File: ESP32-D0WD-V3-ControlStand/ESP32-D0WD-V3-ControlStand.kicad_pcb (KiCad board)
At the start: 2 copper layers, 198.1 x 121.9 mm, 194 parts, among them J1 Button & LED Panel, J10 RJ45, J11 Barrel_Jack, J12 Battery, J13 USB_OTG, J2 Button & LED Panel, J3 STEMMA (Display), J4 Horn, J5 Brake, J6 Light Switch, J7 Reverser, J8 Throttle, J9 RJ45, P1 CONN_8, P2 Misc buttons, bell, status LED, P6 CONN_3, P7 CONN_3, P8 CONN_5, P9 CONN_5, Q1 UMH3N, SW1 A, SW10 SW_PUSH_SMALL, SW11 SW_PUSH_SMALL, SW12 SW_PUSH_SMALL, SW13 SW_PUSH_SMALL, SW14 SW_PUSH_SMALL, SW15 SW_PUSH_SMALL, SW16 SW_PUSH_SMALL, SW17 SW_PUSH_SMALL, SW18 SW_PUSH_SMALL, SW19 SW_PUSH_SMALL, SW2 B, SW20 SW_PUSH_SMALL, SW21 SW_PUSH_SMALL, SW22 SW_PUSH_SMALL, SW23 On/Off, SW24 RESET, SW3 C, SW4 D, SW5 Bell, SW7 SW_PUSH_SMALL, SW8 SW_PUSH_SMALL, SW9 SW_PUSH_SMALL, T1 Buttons, T2 LEDS, T3 Buttons, T4 LEDS, T5 + 15 in -, T6 + 15 out -, U1 MCP23017, U10 ESP32-D0WD-V3, U11 W25Q32JVSSIQ, U2 TBD62083A, U3 MCP23017, U4 TBD62083A, U5 TCAN332DR, U6 MCP73871, U7 LM2574HVM-5.0, U8 TC1263-3.3VOATR, U9 FT231XS-R, Y1 40 Mhz +/- 10 ppm

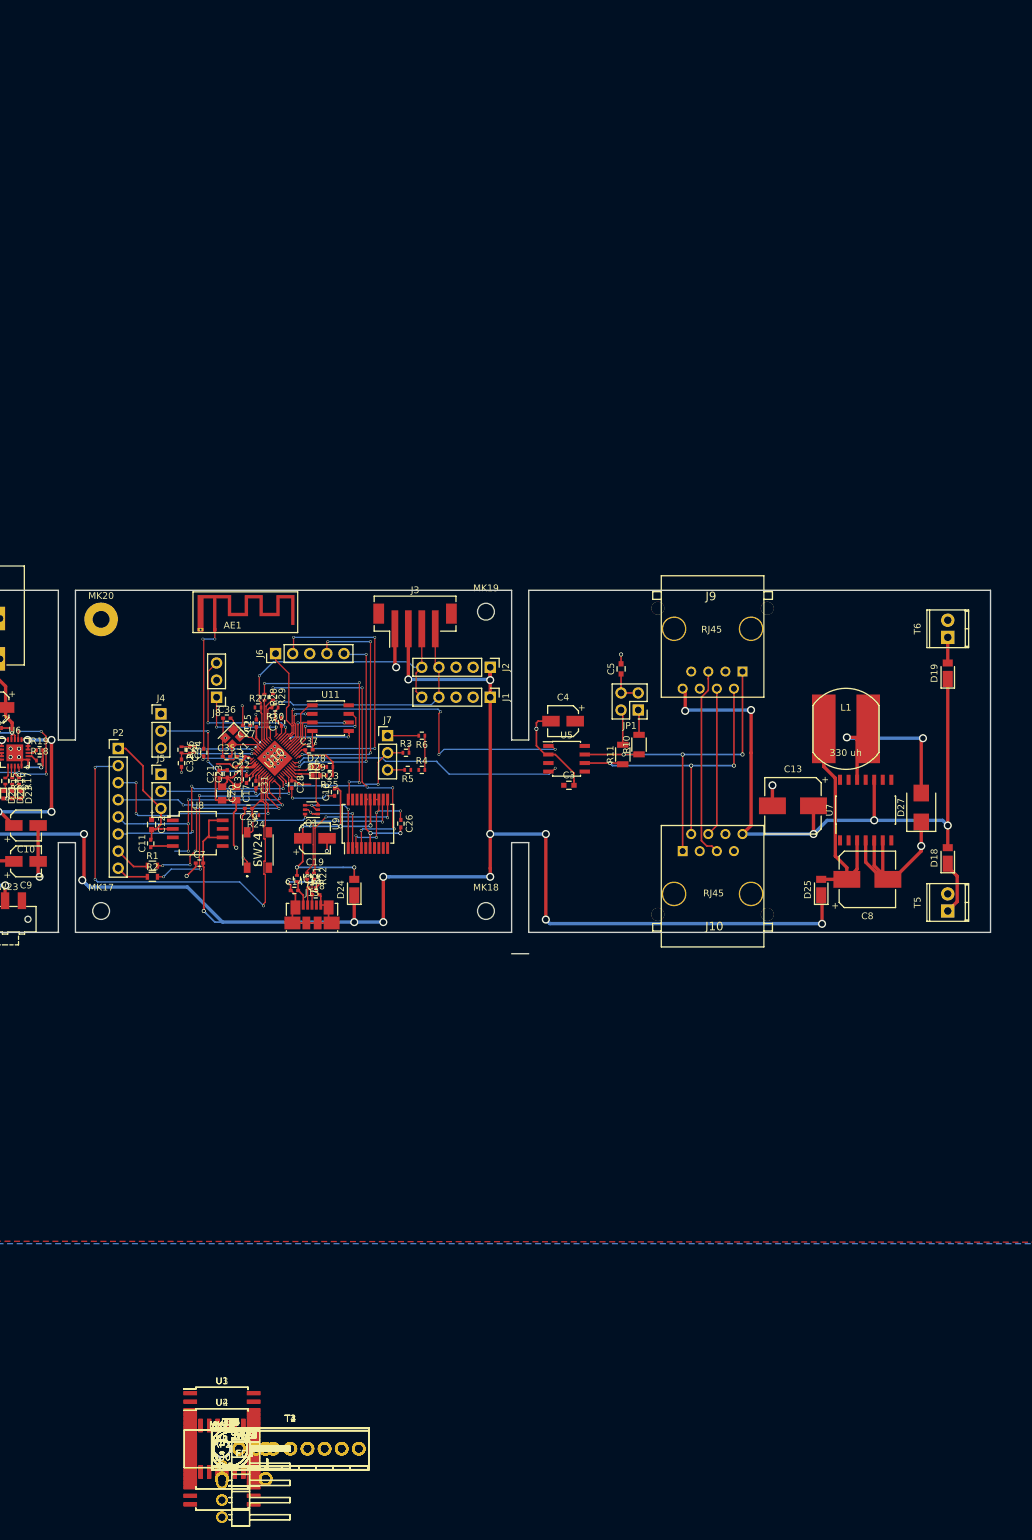
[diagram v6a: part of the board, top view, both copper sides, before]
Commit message: Completed V0-1 board (still need to add a few things -- logos and such and adjust silk).
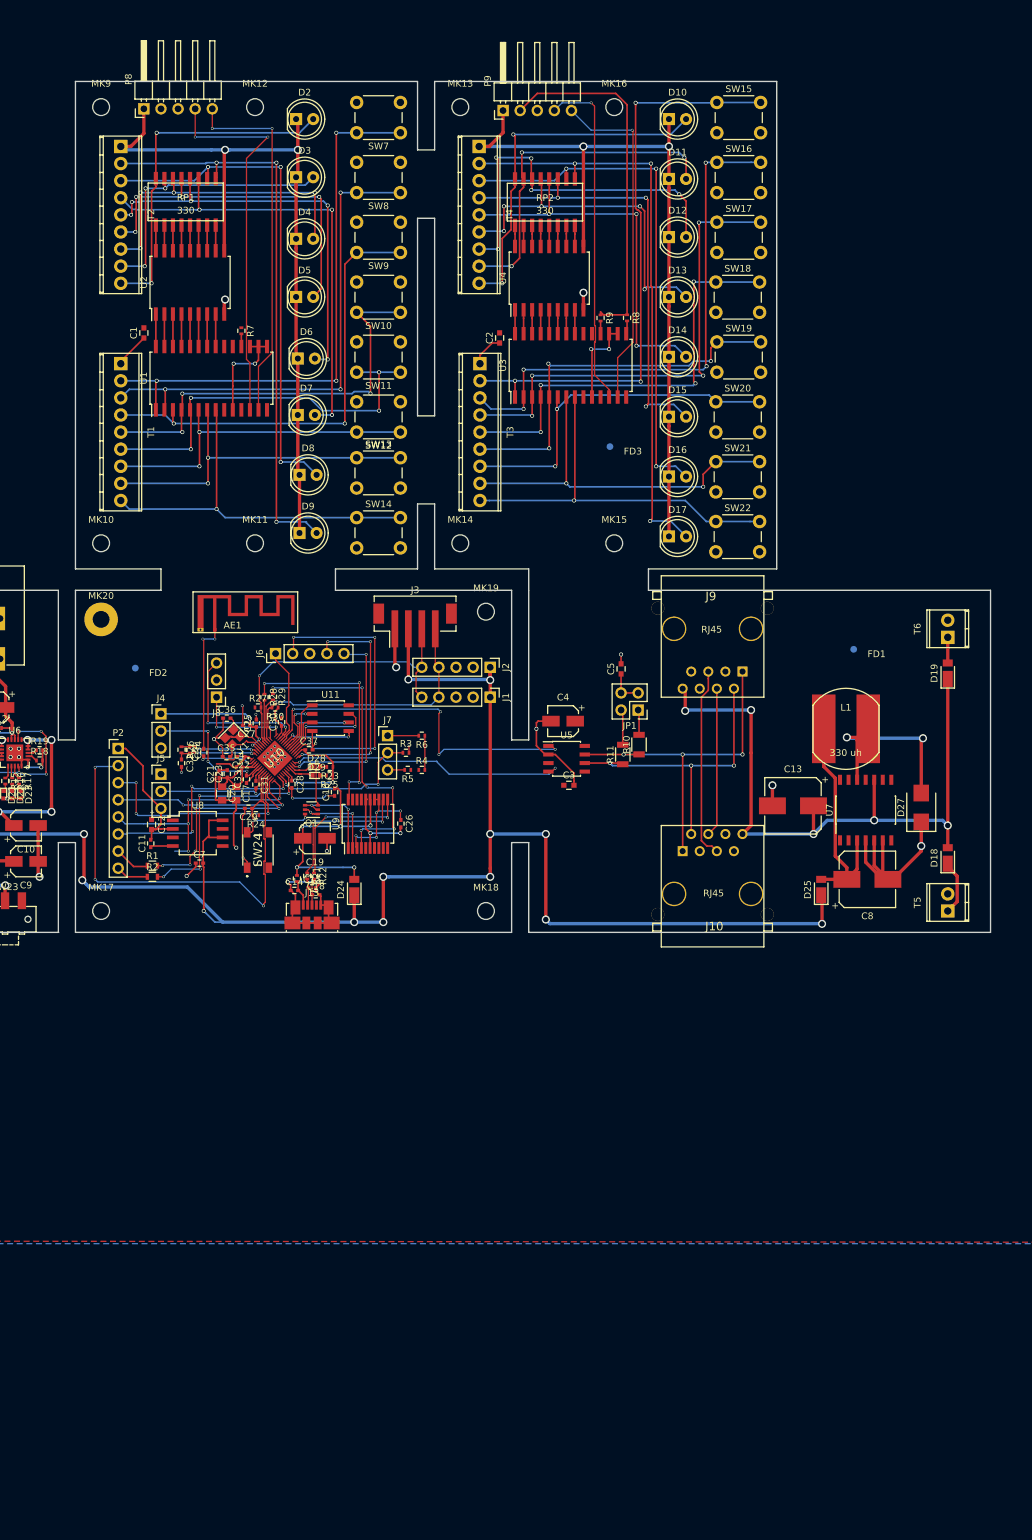
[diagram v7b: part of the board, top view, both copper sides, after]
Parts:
- removed MK21, MK22, MK23, MK24: Mounting_Hole, Mounting_Holes:MountingHole_2.5mm
- moved SW15 213.0 mm to (208.3, 28.5)
- moved D10 208.3 mm to (201.2, 31.0)
- moved MK16 207.6 mm to (193.0, 29.2)
- moved SW16 204.7 mm to (208.3, 37.4)
- moved P9 203.1 mm to (176.5, 29.7), turned to 90 degrees
- moved MK13 202.4 mm to (170.2, 29.2)
- moved MK9 200.0 mm to (116.8, 29.2)
- moved D11 199.9 mm to (201.2, 39.9)
- moved P8 199.3 mm to (123.2, 29.5), turned to 90 degrees
- moved MK12 199.3 mm to (139.7, 29.2)
- moved D2 197.8 mm to (145.8, 31.0)
- moved SW7 197.2 mm to (161.3, 33.0), turned to 180 degrees
- moved T4 197.1 mm to (173.0, 35.1), turned to 270 degrees
- moved SW17 196.4 mm to (208.3, 46.3)
- moved T2 194.0 mm to (119.8, 35.1), turned to 270 degrees
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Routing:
- net +BATT: track 0.00 -> 224.0 mm, vias 0 -> 4
- net Net-(D17-Pad2): track 0.00 -> 87.4 mm, vias 0 -> 3
- net Net-(SW15-Pad1): track 0.00 -> 86.7 mm, vias 0 -> 3
- net Net-(D9-Pad2): track 0.00 -> 85.7 mm, vias 0 -> 3
- net Net-(SW7-Pad1): track 0.00 -> 82.7 mm, vias 0 -> 3
- net Net-(SW16-Pad1): track 0.00 -> 78.8 mm, vias 0 -> 4
- net Net-(D16-Pad2): track 0.00 -> 77.8 mm, vias 0 -> 3
- net Net-(D8-Pad2): track 0.00 -> 76.3 mm, vias 0 -> 3
- net Net-(SW8-Pad1): track 0.00 -> 74.4 mm, vias 0 -> 3
- net +3V3: track 32.4 -> 106.1 mm, vias 2 -> 5
- net Net-(SW17-Pad1): track 0.00 -> 71.4 mm, vias 0 -> 4
- net Net-(D7-Pad2): track 0.00 -> 69.8 mm, vias 0 -> 3
- net Net-(SW9-Pad1): track 0.00 -> 68.5 mm, vias 0 -> 2
- net Net-(D15-Pad2): track 0.00 -> 65.7 mm, vias 0 -> 3
- net Net-(SW18-Pad1): track 0.00 -> 64.2 mm, vias 0 -> 4
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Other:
- board size 198.1 x 121.9 mm -> 198.1 x 126.4 mm

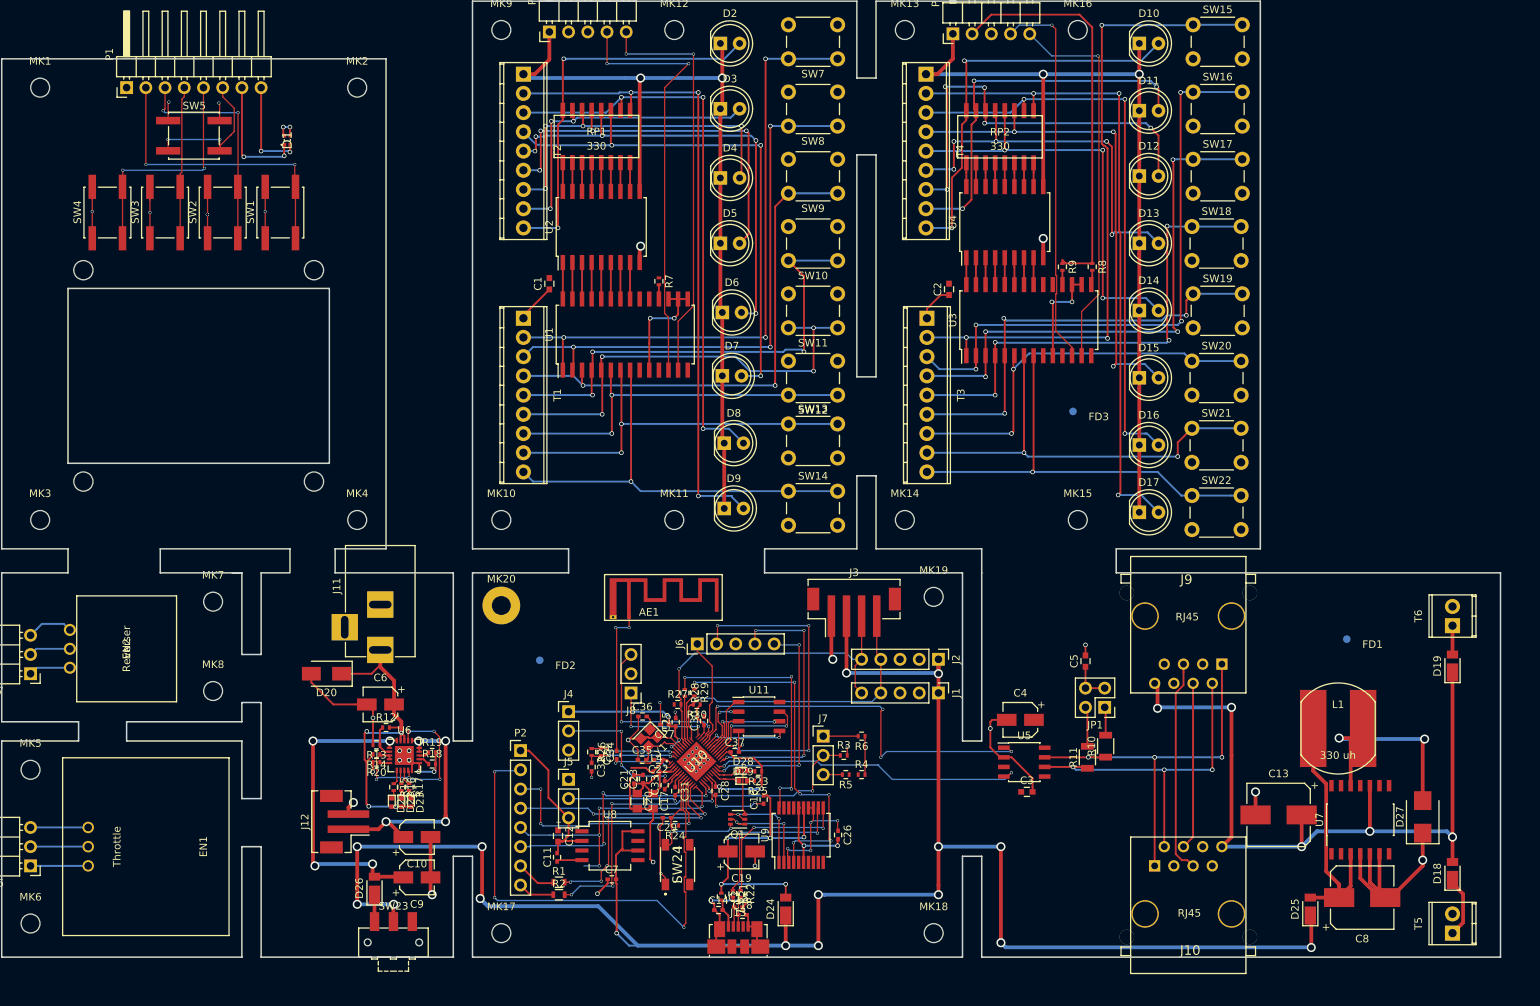
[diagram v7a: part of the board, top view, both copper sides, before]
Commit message: Completed V0-1 board -- added logos, cleaned up silk, added connector labels, etc.
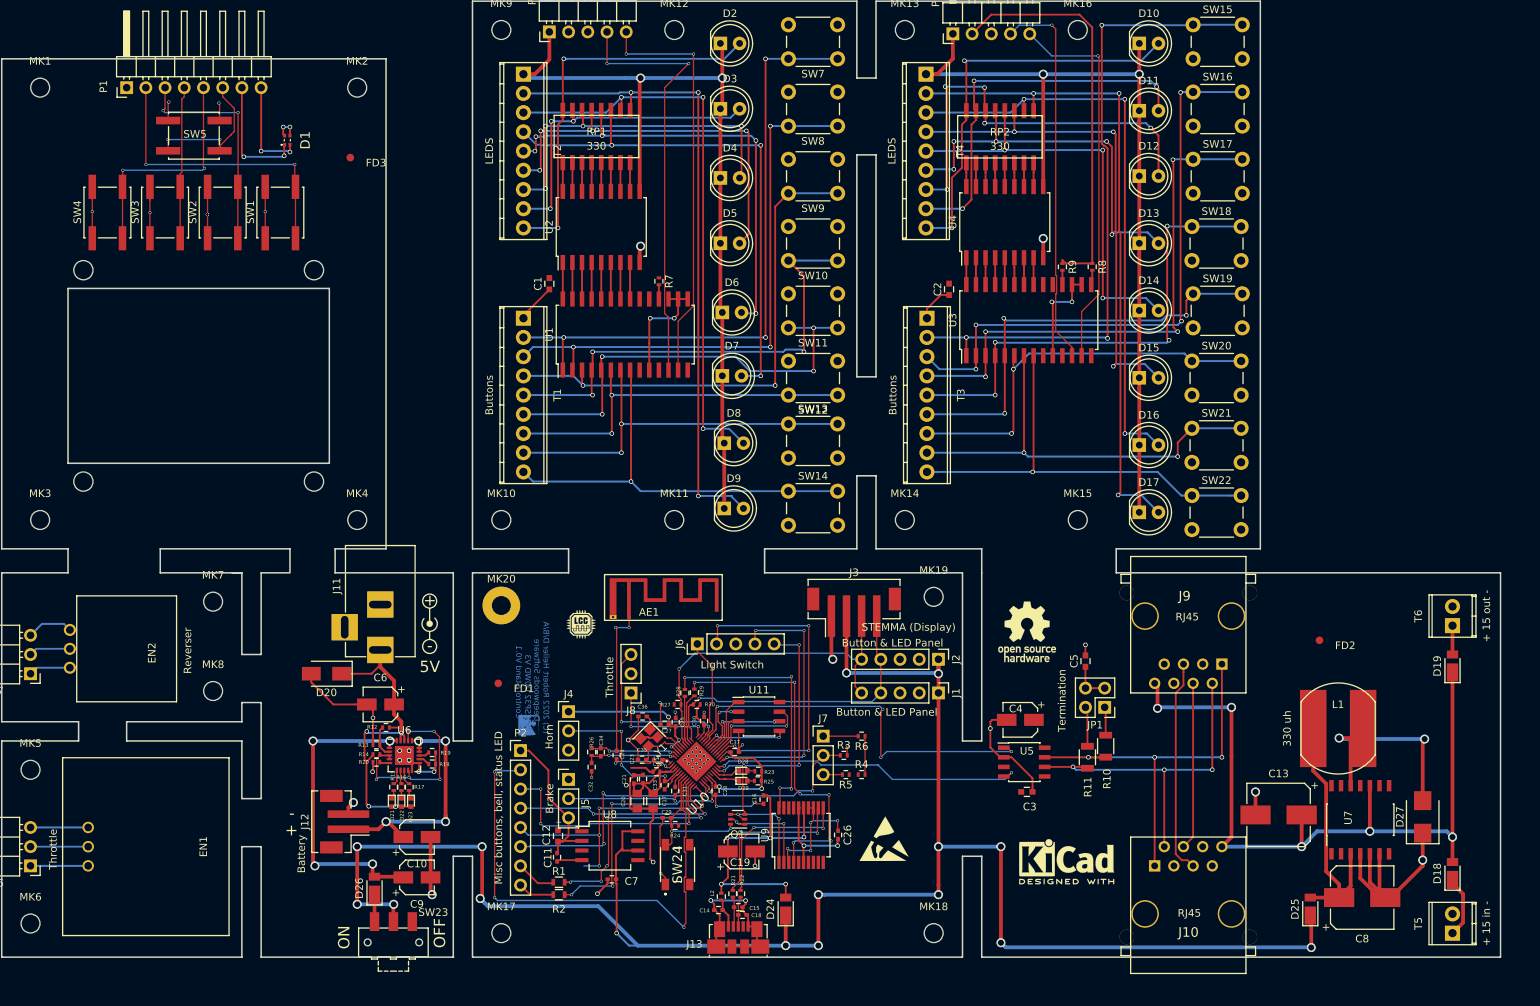
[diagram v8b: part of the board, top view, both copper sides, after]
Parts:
- added ?: , DWSLogoBCU:DWSLogoBCU, F.Cu at (120.4, 121.1)
- added G***: LCC, LCC_LOGO:LCC_LOGO_4.5x4.5, F.Cu at (127.4, 107.7)
- added REF**: Symbol_Barrel_Polarity, Symbols:Symbol_Barrel_Polarity, F.Cu at (107.3, 107.7)
- added REF***: ESD-Logo_6.6x6mm_SilkScreen, Symbols:ESD-Logo_6.6x6mm_SilkScreen, F.Cu at (167.4, 136.1)
- added REF***: KiCad-Logo2_6mm_SilkScreen, Symbols:KiCad-Logo2_6mm_SilkScreen, F.Cu at (191.6, 139.1)
- added REF***: OSHW-Logo_7.5x8mm_SilkScreen, Symbols:OSHW-Logo_7.5x8mm_SilkScreen, F.Cu at (186.3, 108.8)
- FD1, FD2, FD3: footprint Fiducials:Fiducial_1mm_Dia_2.54mm_Outer_CopperBottom -> Fiducials:Fiducial_1mm_Dia_2.54mm_Outer_CopperTop
- moved FD1 112.3 mm to (116.4, 115.6)
- moved FD2 103.1 mm to (225.0, 109.9)
- moved FD3 101.3 mm to (96.9, 46.1)
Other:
- board text added: "(C) 2022 Robert Heller D/B/A Deepwoods Software ESP32 D0WD V3 Control Stand V0.1"
- board text added: "+"
- board text added: "-"
- board text added: "5V"
- board text added: "OFF"
- board text added: "ON"
